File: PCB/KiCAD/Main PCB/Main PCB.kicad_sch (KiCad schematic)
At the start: 37 parts, among them J1 Conn_01x02, J2 Conn_01x02, J3 Conn_01x02, J5 Conn_01x02, J6 Conn_01x04, J7 Conn_01x04, J8 Conn_01x04, Q1 BSS138, Q2 BSS138, U2 Teensy4.1, U3 Teensy4.0, U8 MIC5219-3.3YM5

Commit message: New motor controllers for the main PCB
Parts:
- removed C24, C25: 10uF, Capacitor_Tantalum_SMD:CP_EIA-3216-12_Kemet-S_Pad1.58x1.35mm_HandSolder, symbol Device:C_Polarized
- removed C26: 0.1uF, Capacitor_SMD:C_0805_2012Metric_Pad1.18x1.45mm_HandSolder, symbol Device:C
- removed F1: Fuse, Fuse:Fuseholder_Blade_Mini_Keystone_3568, symbol Device:Fuse
- removed J1: Conn_01x02, Connector_AMASS:AMASS_XT60-M_1x02_P7.20mm_Vertical, symbol Connector_Generic:Conn_01x02
- removed J5: Conn_01x02, Connector_JST:JST_PH_B2B-PH-K_1x02_P2.00mm_Vertical, symbol Connector_Generic:Conn_01x02
- removed S2: 1101M2S3CGE2, 1101M2S3CGE2:1101M2S3CGE2, symbol 1101M2S3CGE2:1101M2S3CGE2
- removed U1: ~, Pololu:D36V28F5, symbol Pololu:D36V28F5
- removed U8: MIC5219-3.3YM5, Package_TO_SOT_SMD:SOT-23-5, symbol Regulator_Linear:MIC5219-3.3YM5
- added J3: Conn_01x04, Connector_JST:JST_PH_B4B-PH-K_1x04_P2.00mm_Vertical, symbol Connector_Generic:Conn_01x04
- renumbered J6 to J1, J7 to J2, J8 to J4, J2 to J5, J3 to J6, R12 to R10, R13 to R11, R14 to R12, R9 to R13, R10 to R14, R7 to R3, R8 to R4, R3 to R5, R4 to R6, R5 to R7, R6 to R8, R11 to R9, S3 to S2, S4 to S3, U2 to U1, U3 to U2
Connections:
- net IR_DIR_112.5 is gone; now on net IR_DIR_180: U1.27 (35_TX8)
- net IR_DIR_157.5 is gone; now on net IR_DIR_270: U1.28 (36_CS)
- net IR_DIR_202.5 is gone; now on net IR_DIR_45: U1.29 (37_CS)
- net IR_DIR_22.5 is gone; now on net IR_DIR_0: U1.25 (33_MCLK2)
- net IR_DIR_247.5 is gone; now on net IR_DIR_135: U1.30 (38_CS1_IN1)
- net IR_DIR_292.5 is gone; now on net IR_DIR_225: U1.31 (39_MISO1_OUT1A)
- net IR_DIR_337.5 is gone; now on net IR_DIR_315: U1.32 (40_A16)
- net IR_DIR_67.5 is gone; now on net IR_DIR_90: U1.26 (34_RX8)
- net MOTOR_1_DIR is gone; now on net LED_1_A1: U2.5 (3_LRCLK2)
- net MOTOR_1_SPEED is gone; now on net LED_1_A0: U2.4 (2_OUT2)
- net MOTOR_2_DIR is gone; now on net LED_2_A0: U2.7 (5_IN2)
- net MOTOR_2_SPEED is gone; now on net LED_1_A2: U2.6 (4_BCLK2)
- net MOTOR_3_DIR is gone; now on net LED_2_A2: U2.9 (7_RX2_OUT1A)
- net MOTOR_3_SPEED is gone; now on net LED_2_A1: U2.8 (6_OUT1D)
- net STATUS_GREEN_4_0 is gone; now on net LED_1_OUT: U2.21 (14_A0_TX3_SPDIF_OUT)
- net +3V3: now also J4.1 (Pin_1), R1.2, R2.2, R5.2, R6.2, R7.2, R8.2, S2.2, S3.2; no longer R1.1, R2.1, R5.1, R6.1, R7.1, R8.1
- net COM_RX: now also U1.38 (16_A2_RX4_SCL1); no longer U1.43 (21_A7_RX5_BCLK1)
- net COM_TX: now also U1.39 (17_A3_TX4_SDA1); no longer U1.42 (20_A6_TX5_LRCLK1)
- net IR_DIR_0: no longer U1.4 (2_OUT2)
- net IR_DIR_135: no longer U1.36 (14_A0_TX3_SPDIF_OUT)
- net IR_DIR_180: no longer U1.6 (4_BCLK2)
- net IR_DIR_225: no longer U1.37 (15_A1_RX3_SPDIF_IN)
- net IR_DIR_270: no longer U1.7 (5_IN2)
- net IR_DIR_315: no longer U1.38 (16_A2_RX4_SCL1)
- net IR_DIR_45: no longer U1.14 (12_MISO_MQSL)
- net IR_DIR_90: no longer U1.5 (3_LRCLK2)
- net LED_1_A0: no longer U2.13 (11_MOSI_CTX1)
- net LED_1_A1: no longer U2.14 (12_MISO_MQSL)
- net LED_1_A2: no longer U2.23 (16_A2_RX4_SCL1)
- net LED_1_OUT: no longer U2.12 (10_CS_MQSR)
- net LED_2_A0: no longer U2.27 (20_A6_TX5_LRCLK1)
- net LED_2_A1: no longer U2.28 (21_A7_RX5_BCLK1)
- net LED_2_A2: no longer U2.35 (24_A10_TX6_SCL2)
- net LED_2_OUT: now also U2.22 (15_A1_RX3_SPDIF_IN); no longer U2.24 (17_A3_TX4_SDA1)
- net LG_RECEIVE: now also U1.42 (20_A6_TX5_LRCLK1); no longer U2.22 (15_A1_RX3_SPDIF_IN)
- net TSSP_1_A0: now also U2.13 (11_MOSI_CTX1); no longer U2.39 (28_RX7)
- net TSSP_1_A1: now also U2.14 (12_MISO_MQSL); no longer U2.40 (29_TX7)
- net TSSP_1_A2: now also U2.28 (21_A7_RX5_BCLK1); no longer U2.41 (30_CRX3)
- net TSSP_1_OUT: now also U2.24 (17_A3_TX4_SDA1); no longer U2.29 (22_A8_CTX1)
- net TSSP_2_A0: now also U2.29 (22_A8_CTX1); no longer U2.42 (31_CTX3)
- net TSSP_2_A1: now also U2.30 (23_A9_CRX1_MCLK1); no longer U2.43 (32_OUT1B)
- net TSSP_2_A2: now also U2.37 (26_A12_MOSI1); no longer U2.44 (33_MCLK2)
- net TSSP_2_OUT: now also U2.27 (20_A6_TX5_LRCLK1); no longer U2.30 (23_A9_CRX1_MCLK1)
- net at S1.B3, U1.21 (29_TX7): now also R5.1; no longer R5.2
- net at S1.B4, U1.22 (30_CRX3): now also R6.1; no longer R6.2
- net at S1.B2, U1.20 (28_RX7): now also R2.1; no longer R2.2
- net PWM_M4: now reaches U1.16 (24_A10_TX6_SCL2)
- net IN_A_M4: now reaches U1.17 (25_A11_RX6_SDA2)
- net IN_B_M4: now reaches U1.18 (26_A12_MOSI1)
- net at S1.B1, U1.19 (27_A13_SCK1): now also R1.1; no longer R1.2
- net at S1.B5, U1.23 (31_CTX3): now also R7.1; no longer R7.2
- net at S1.B6, U1.24 (32_OUT1B): now also R8.1; no longer R8.2
- net IN_A_M3: now reaches U1.44 (22_A8_CTX1)
- net PWM_M3: now reaches U1.45 (23_A9_CRX1_MCLK1)
- net IN_B_M2: now reaches U1.8 (6_OUT1D)
- net +3V3_4_0: no longer names the net of U2.31 (3V3)
- net +3V3_4_0: no longer J4.1 (Pin_1)
- removed net +3V3_4_1: S2.2, S3.2, U1.46 (3V3)
- net MOTOR_4_DIR renamed LED_3_A1
- net LED_3_A1: now also J3.3 (Pin_3)
- net MOTOR_4_SPEED renamed LED_3_A0
- net LED_3_A0: now also J3.2 (Pin_2)
- net STATUS_GREEN_4_1 renamed STATUS_GREEN_MAIN
- net STATUS_RED_4_0 renamed STATUS_RED_TEENSY_1
- net STATUS_RED_4_1 renamed STATUS_RED_MAIN
- net TEENSY_RX renamed TEENSY_1_RX
- net TEENSY_TX renamed TEENSY_1_TX
- new net IN_A_M1: U1.5 (3_LRCLK2)
- new net IN_A_M2: U1.7 (5_IN2)
- new net IN_B_M1: U1.6 (4_BCLK2)
- new net IN_B_M3: U1.43 (21_A7_RX5_BCLK1)
- new net LED_3_A2: J3.4 (Pin_4), U2.12 (10_CS_MQSR)
- new net LED_3_OUT: J3.1 (Pin_1), U2.23 (16_A2_RX4_SCL1)
- new net PWM_M1: U1.4 (2_OUT2)
- new net PWM_M2: U1.14 (12_MISO_MQSL)
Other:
- added sheet Power (power.kicad_sch)
- moved on the sheet: CAM1, CAM2, J1, J2, J4, J5, J6, Q1, Q2, R1, R10, R11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

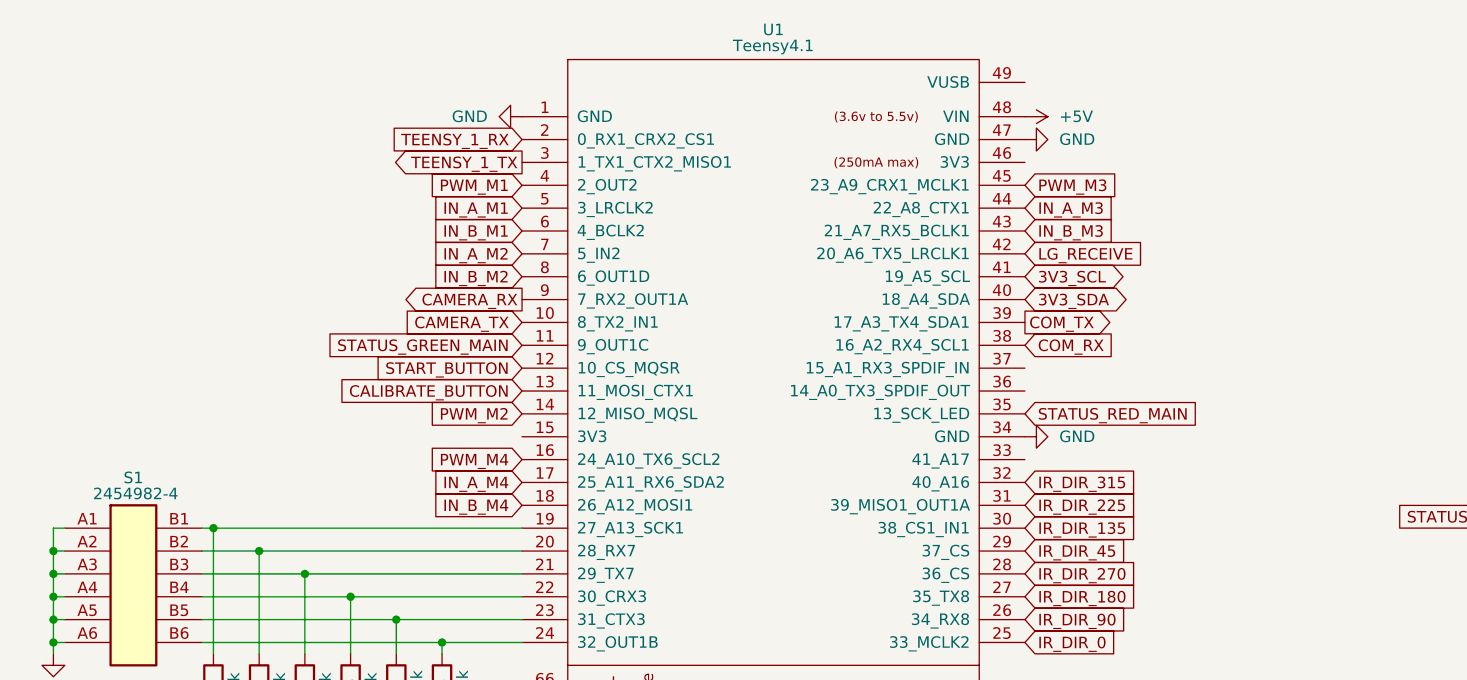
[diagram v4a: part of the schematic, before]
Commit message: Added a dribbler motor controller
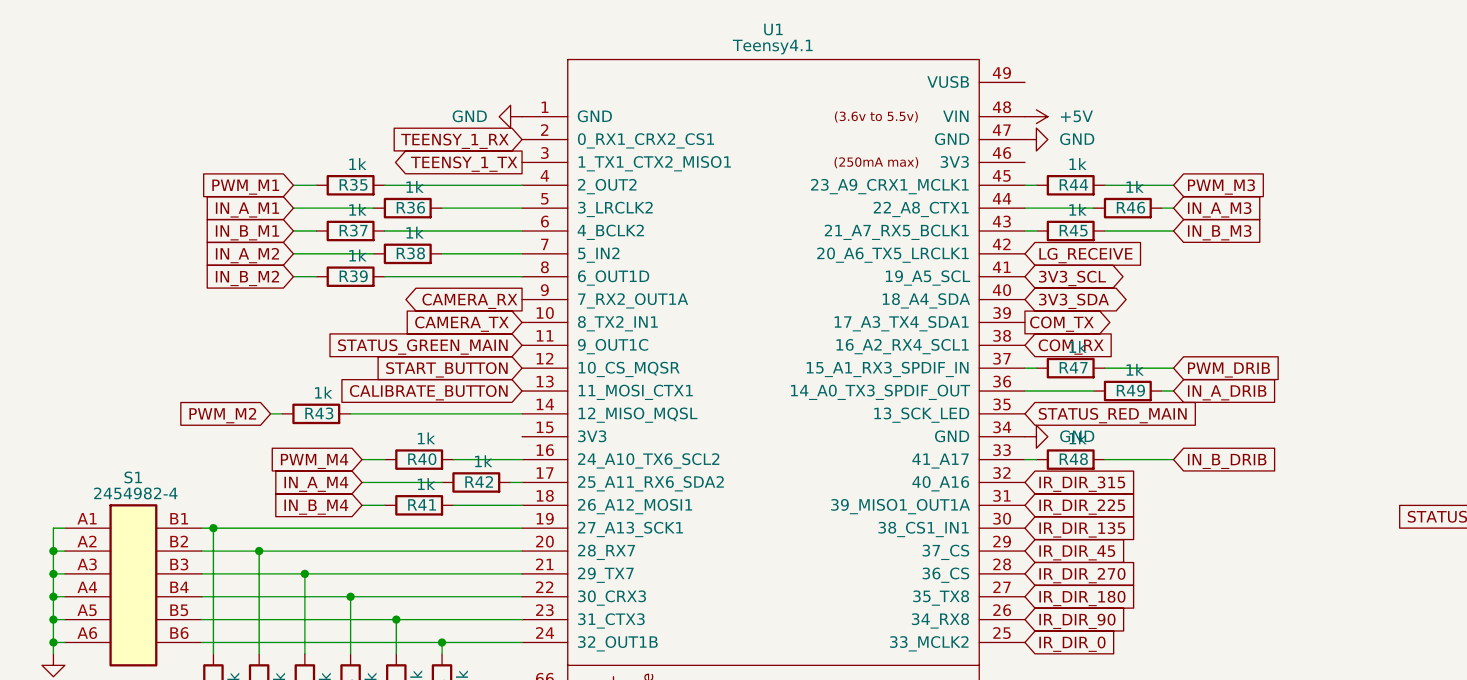
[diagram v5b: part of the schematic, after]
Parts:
- added R35, R36, R37, R38, R39, R40, R41, R42, R43, R44, R45, R46, R47, R48, R49: 1k, Resistor_SMD:R_0805_2012Metric_Pad1.20x1.40mm_HandSolder, symbol Device:R
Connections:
- net IN_A_M1: now also R36.1; no longer U1.5 (3_LRCLK2)
- net IN_A_M2: now also R38.1; no longer U1.7 (5_IN2)
- net IN_A_M3: now also R46.2; no longer U1.44 (22_A8_CTX1)
- net IN_A_M4: now also R42.1; no longer U1.17 (25_A11_RX6_SDA2)
- net IN_B_M1: now also R37.1; no longer U1.6 (4_BCLK2)
- net IN_B_M2: now also R39.1; no longer U1.8 (6_OUT1D)
- net IN_B_M3: now also R45.2; no longer U1.43 (21_A7_RX5_BCLK1)
- net IN_B_M4: now also R41.1; no longer U1.18 (26_A12_MOSI1)
- net PWM_M1: now also R35.1; no longer U1.4 (2_OUT2)
- net PWM_M2: now also R43.1; no longer U1.14 (12_MISO_MQSL)
- net PWM_M3: now also R44.2; no longer U1.45 (23_A9_CRX1_MCLK1)
- net PWM_M4: now also R40.1; no longer U1.16 (24_A10_TX6_SCL2)
- net at U1.33 (41_A17): now also R48.1
- net at U1.36 (14_A0_TX3_SPDIF_OUT): now also R49.1
- net at U1.37 (15_A1_RX3_SPDIF_IN): now also R47.1
- new net: R36.2, U1.5 (3_LRCLK2)
- new net: R42.2, U1.17 (25_A11_RX6_SDA2)
- new net: R45.1, U1.43 (21_A7_RX5_BCLK1)
- new net: R40.2, U1.16 (24_A10_TX6_SCL2)
- new net: R43.2, U1.14 (12_MISO_MQSL)
- new net: R35.2, U1.4 (2_OUT2)
- new net: R41.2, U1.18 (26_A12_MOSI1)
- new net: R39.2, U1.8 (6_OUT1D)
- new net: R44.1, U1.45 (23_A9_CRX1_MCLK1)
- new net: R37.2, U1.6 (4_BCLK2)
- new net: R38.2, U1.7 (5_IN2)
- new net: R46.1, U1.44 (22_A8_CTX1)
- new net IN_A_DRIB: R49.2
- new net IN_B_DRIB: R48.2
- new net PWM_DRIB: R47.2

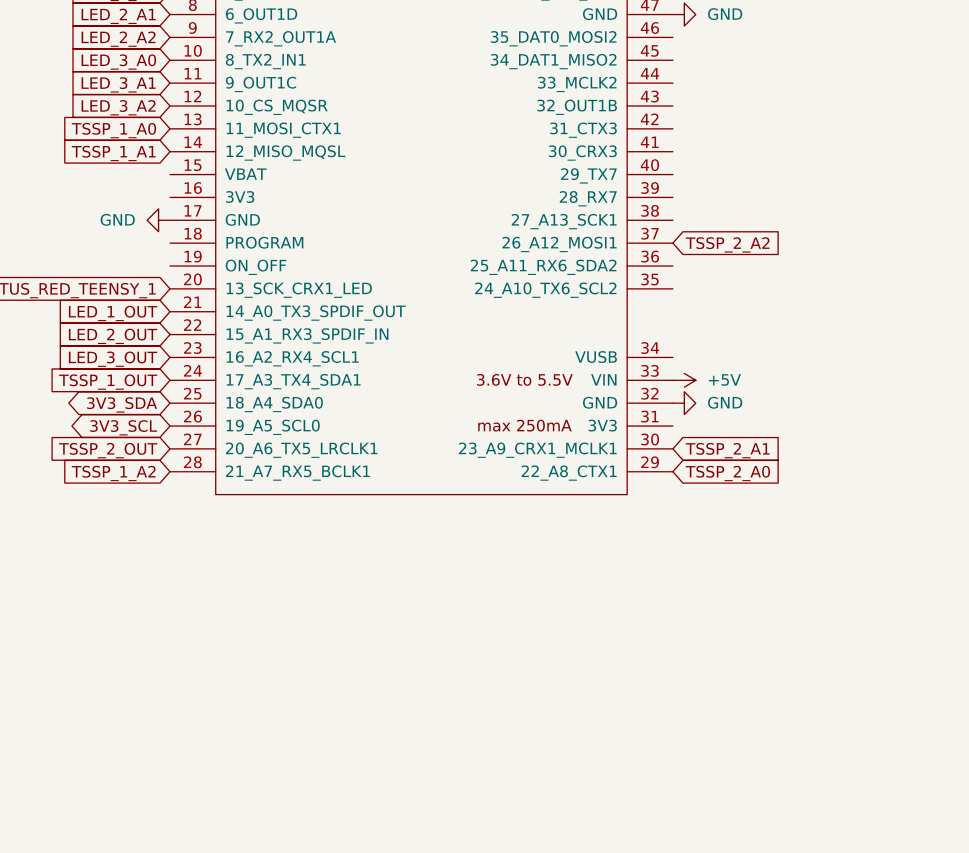
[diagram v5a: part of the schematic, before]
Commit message: Added kicker and spare serial and i2c
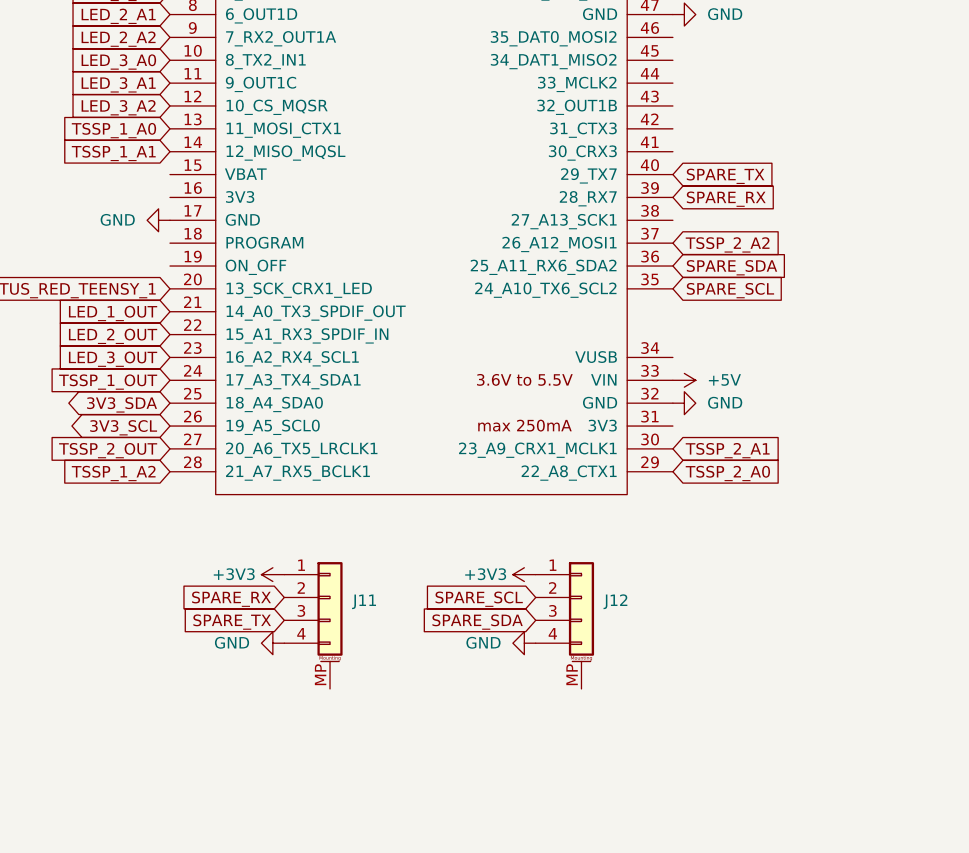
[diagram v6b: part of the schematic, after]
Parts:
- added J11, J12: Conn_01x04_MountingPin, Connector_JST:JST_PH_S4B-PH-SM4-TB_1x04-1MP_P2.00mm_Horizontal, symbol Connector_Generic_MountingPin:Conn_01x04_MountingPin
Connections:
- net +3V3: now also J11.1 (Pin_1), J12.1 (Pin_1)
- net GND: now also J11.4 (Pin_4), J12.4 (Pin_4)
- net SPARE_SCL: now reaches U2.35 (24_A10_TX6_SCL2)
- net SPARE_SCL: now also J12.2 (Pin_2)
- net SPARE_SDA: now reaches U2.36 (25_A11_RX6_SDA2)
- net SPARE_SDA: now also J12.3 (Pin_3)
- net SPARE_RX: now reaches U2.39 (28_RX7)
- net SPARE_RX: now also J11.2 (Pin_2)
- net SPARE_TX: now reaches U2.40 (29_TX7)
- net SPARE_TX: now also J11.3 (Pin_3)
